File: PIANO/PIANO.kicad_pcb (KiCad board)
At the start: 2 copper layers, 71.6 x 47.5 mm, 31 parts, among them SW1 ON/OFF, SW2 RESET, U1 LF33_TO220, U2 ESP32-S2-SOLO, U3 Opamp_Dual, U4 Opamp_Dual

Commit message: During Class Commit
This contains all changes before design review
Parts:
- U1: value LF33_TO220 -> LDO 3.3V
- moved R2 2.18 mm to (153.5, 96.1)
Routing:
- net Net-(R2-Pad2): track 7.26 -> 15.8 mm, vias 0 -> 2
- net GND: track 0.00 -> 7.31 mm, vias 0 -> 4
- net Net-(C4-Pad1): track 15.9 -> 20.5 mm
- net /IO0: track 32.8 -> 37.0 mm
- net Net-(RV3-Pad2): track 35.9 -> 39.7 mm
- net Net-(R2-Pad1): track 19.5 -> 23.1 mm
- net +3V3: track 73.9 -> 76.6 mm
- net /Output: track 73.5 -> 76.0 mm
- net Net-(RV2-Pad2): track 16.4 -> 18.1 mm
- net +5V: track 66.6 -> 68.1 mm
- net Net-(C3-Pad2): track 24.3 -> 25.4 mm
- net /En: track 14.1 -> 13.4 mm

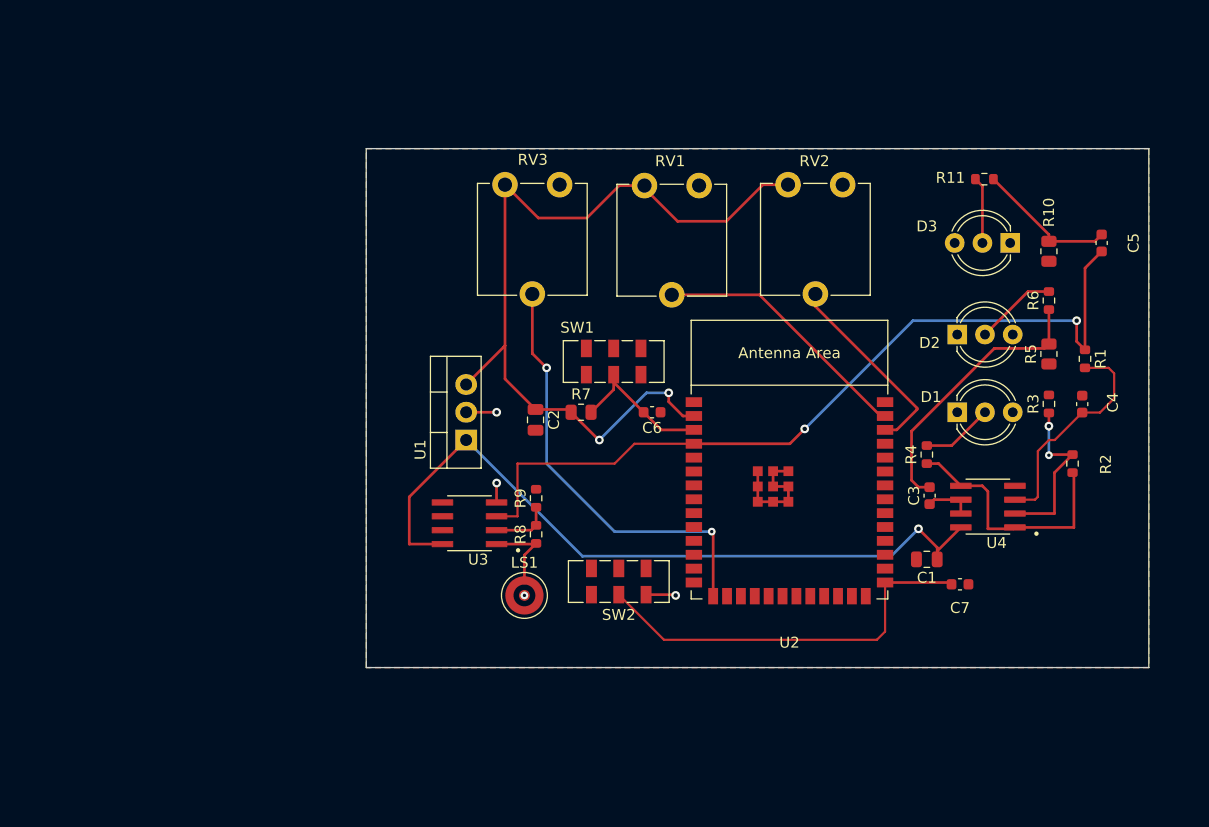
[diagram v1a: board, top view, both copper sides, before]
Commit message: Final Handoff to Wesley
Corrected units, created exclusion, thickened traces
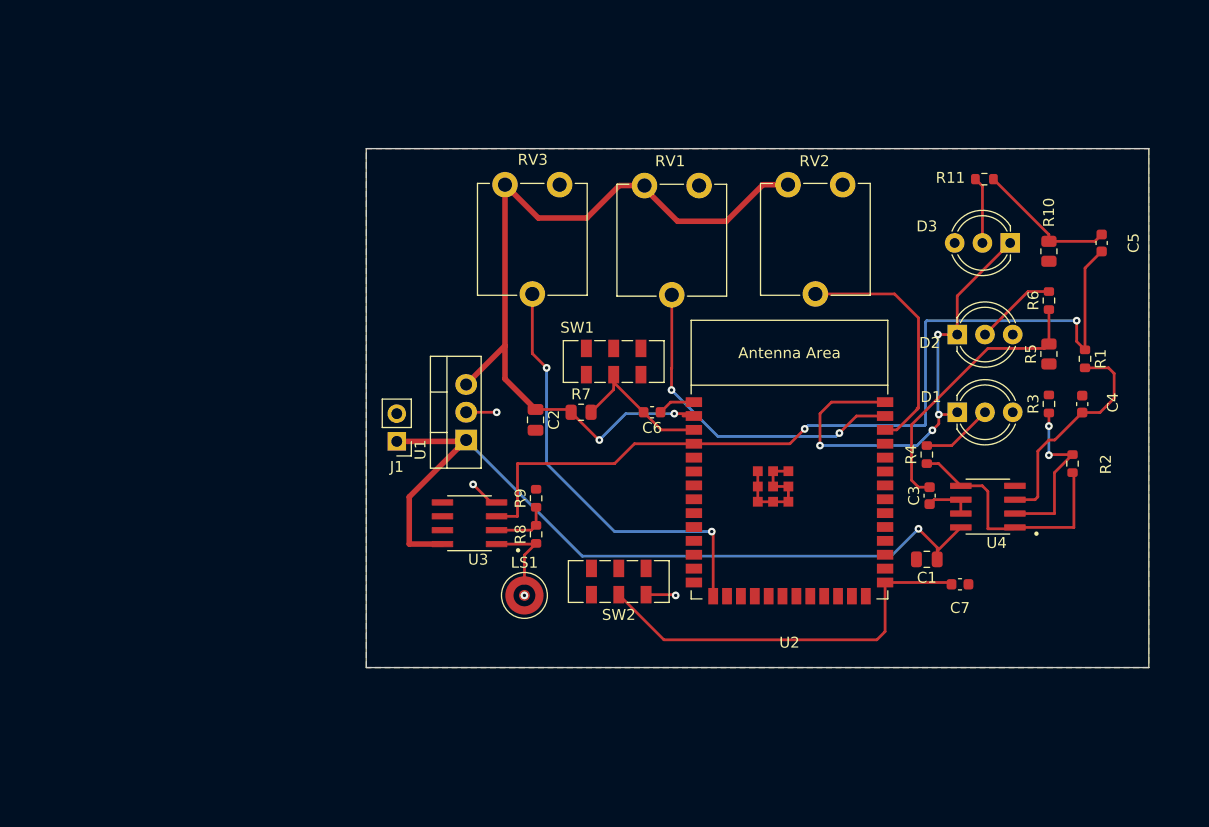
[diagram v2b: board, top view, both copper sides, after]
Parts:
- added J1: Conn_01x02_Male, Connector_PinHeader_2.54mm:PinHeader_1x02_P2.54mm_Vertical, F.Cu at (91.7, 94.1)
- C1, C2: value 10 mF -> 10 uF
- C3, C5, C6, C7: value .1 mF -> .1 uF
- C4: value .4 mF -> .4 uF
- U1: value LDO 3.3V -> LF33_TO220
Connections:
- U2 pad 40: unconnected-(U2-Pad40) -> GND
- U2 pad 41: unconnected-(U2-Pad41) -> GND
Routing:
- net GND: track 7.31 -> 66.5 mm, vias 4 -> 8
- net unconnected-(U2-Pad41): track 11.2 -> 0.00 mm
- net Net-(RV1-Pad2): track 24.1 -> 30.8 mm, vias 0 -> 2
- net +5V: track 68.1 -> 74.5 mm
- net /Output: track 76.0 -> 81.5 mm
- net Net-(RV2-Pad2): track 18.1 -> 22.6 mm
- net +3V3: track 76.6 -> 75.6 mm

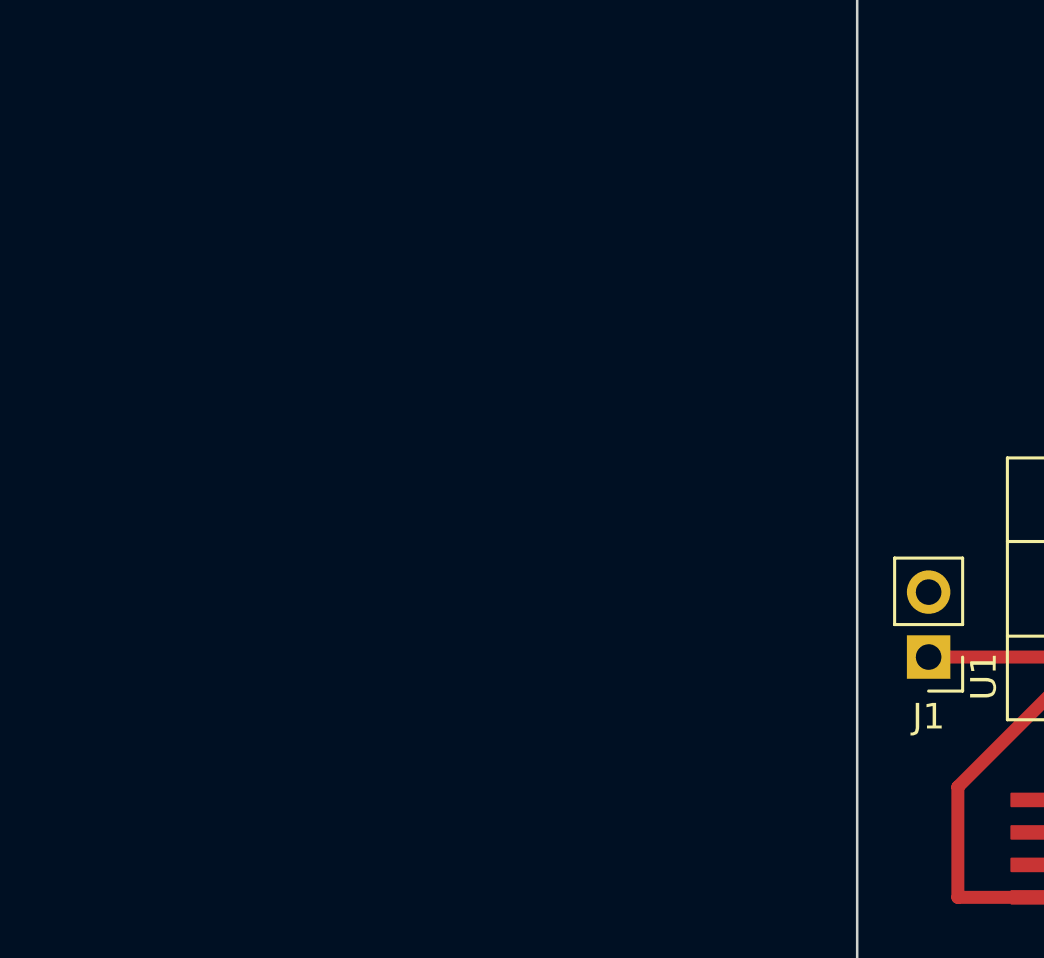
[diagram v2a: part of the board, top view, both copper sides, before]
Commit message: New Power Delivery
Created new switching regulator and respective passives.
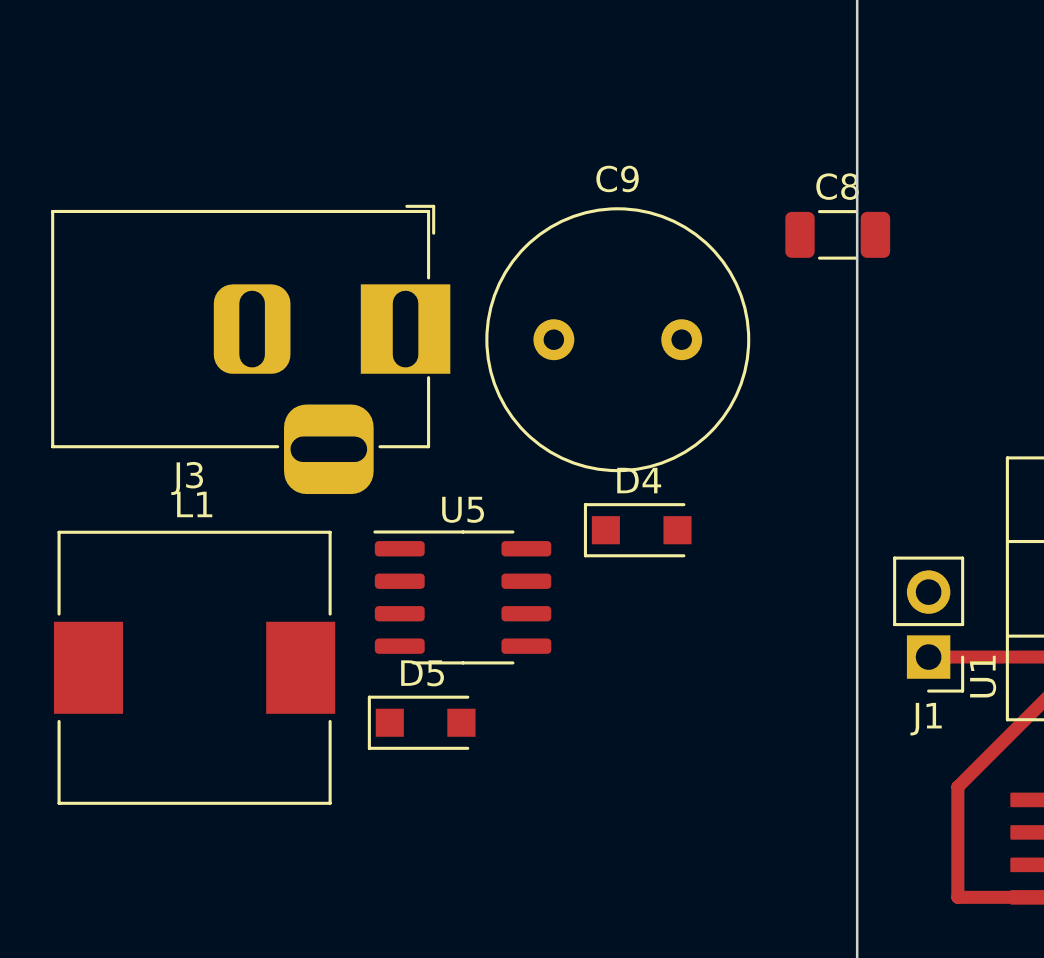
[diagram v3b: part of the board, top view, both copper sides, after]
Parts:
- added C8: 330uF, Capacitor_SMD:C_1206_3216Metric, F.Cu at (88.1, 77.6)
- added C9: 1000uF, Capacitor_THT:C_Radial_D10.0mm_H16.0mm_P5.00mm, F.Cu at (77.0, 81.7)
- added D4: DIODE, Diode_SMD:D_SOD-123F, F.Cu at (80.5, 89.1)
- added D5: D_Schottky, Diode_SMD:D_SOD-123F, F.Cu at (72.0, 96.7)
- added J3: Barrel_Jack_Switch, Connector_BarrelJack:BarrelJack_Horizontal, F.Cu at (71.2, 81.3)
- added L1: 39uH, Inductor_SMD:L_10.4x10.4_H4.8, F.Cu at (63.0, 94.5)
- added U5: AP1509-50SG-13, Package_SO:SOIC-8_3.9x4.9mm_P1.27mm, F.Cu at (73.5, 91.8)
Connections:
- U3 pad 8: +5V -> Net-(U3-Pad8)

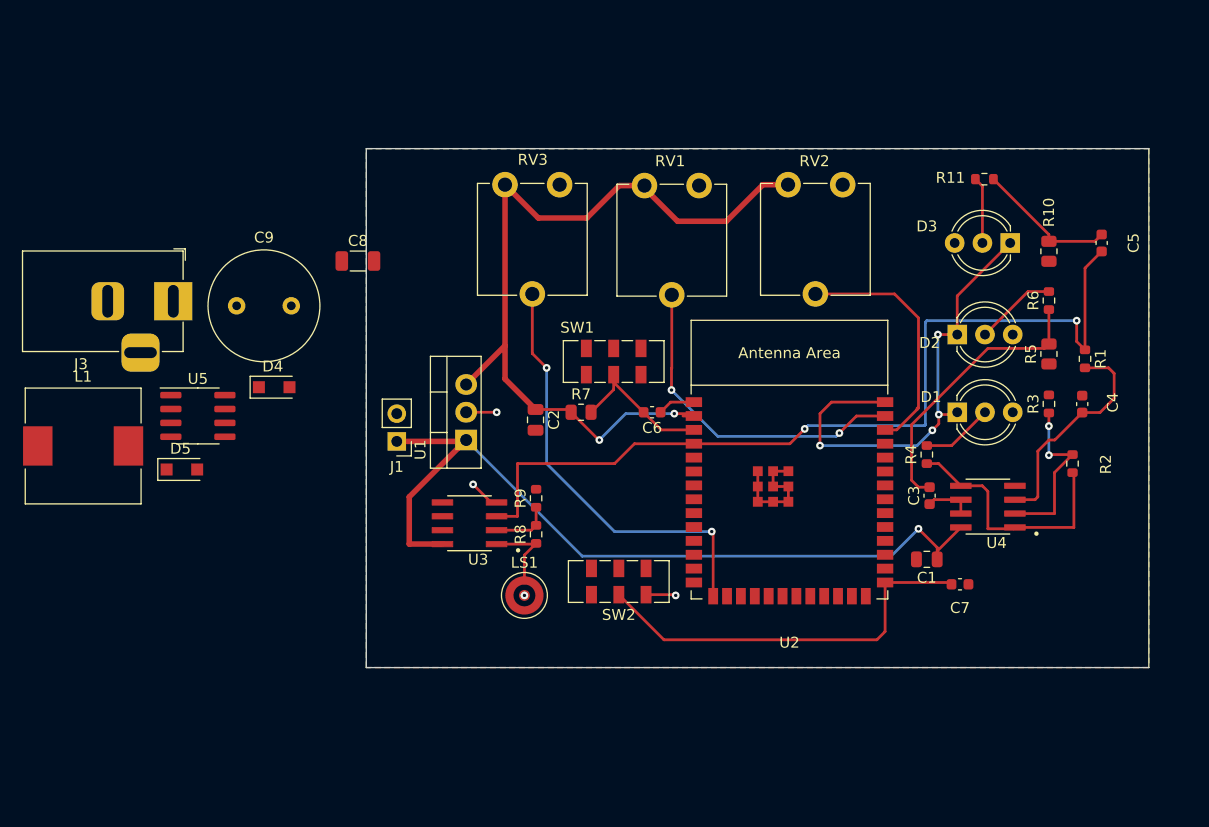
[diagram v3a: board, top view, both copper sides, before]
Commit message: added usb component
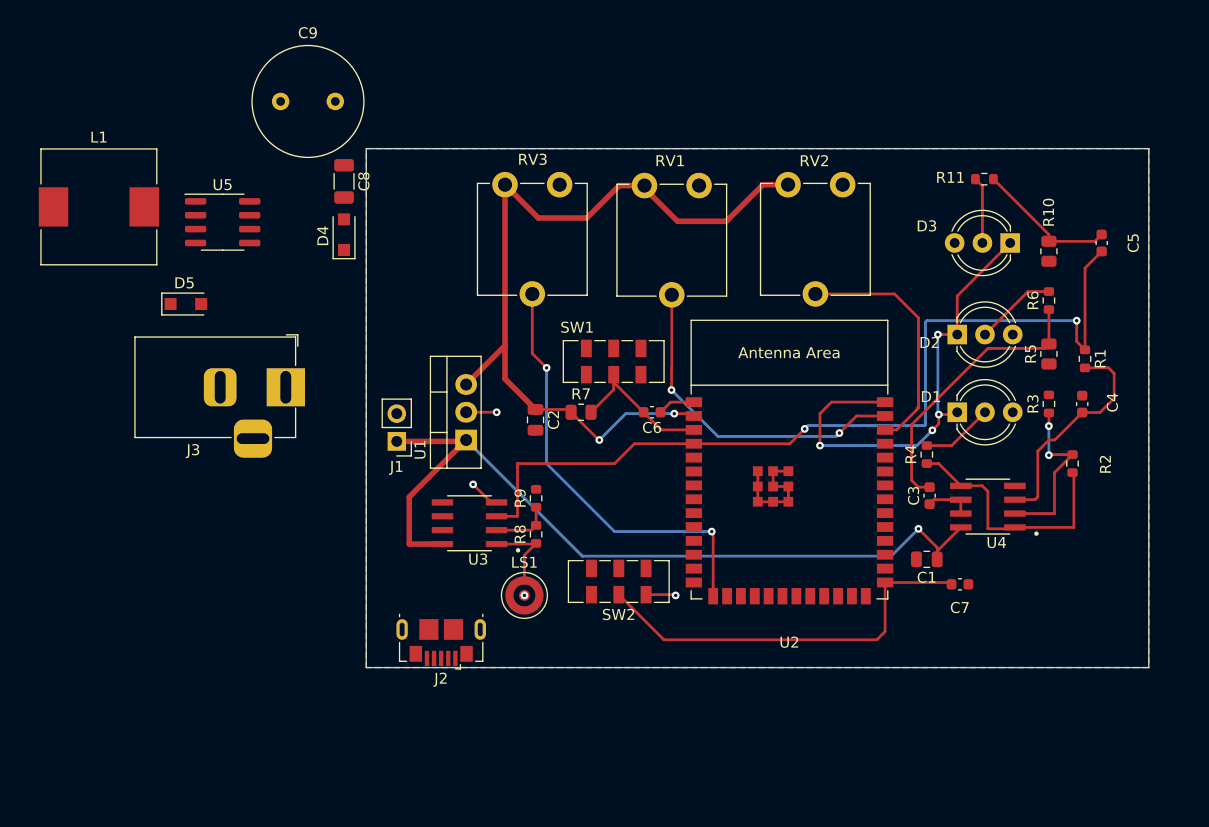
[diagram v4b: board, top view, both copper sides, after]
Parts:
- added J2: USB_B_Micro, Connector_USB:USB_Micro-B_GCT_USB3076-30-A, F.Cu at (95.8, 112.5)
- moved L1 21.9 mm to (64.4, 72.6)
- moved C9 19.1 mm to (81.1, 63.0)
- moved U5 17.9 mm to (75.8, 74.0)
- moved D4 15.4 mm to (86.9, 75.2), turned to 90 degrees
- moved D5 15.1 mm to (72.4, 81.5)
- moved J3 13.0 mm to (81.5, 89.2)
- moved C8 7.40 mm to (86.9, 70.3), turned to -90 degrees
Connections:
- U2 pad 13: unconnected-(U2-Pad13) -> /D-
- U2 pad 14: unconnected-(U2-Pad14) -> /D+
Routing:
- net +3V3: track 75.6 -> 74.6 mm

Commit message: added some stuff
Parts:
- moved J2 1.00 mm to (95.8, 111.5), turned to 0 degrees
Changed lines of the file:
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@@
   )
   (footprint "Connector_USB:USB_Micro-B_GCT_USB3076-30-A" (layer "F.Cu")
-    (at 95.758 112.522 180)
+    (at 95.758 111.52)
     (descr "GCT Micro USB https://gct.co/files/drawings/usb3076.pdf")
     (tags "Micro-USB SMD Typ-B GCT")
@@
     (fp_line (start -1.1 -2.16) (end -1.1 -1.95) (layer "F.Fab") (width 0.1))
     (fp_line (start -1.5 -2.16) (end -1.5 -1.95) (layer "F.Fab") (width 0.1))
-    (pad "1" smd rect (at -1.3 -1.45 180) (size 0.4 1.4) (layers "F.Cu" "F.Paste" "F.Mask")
+    (pad "1" smd rect (at -1.3 -1.45) (size 0.4 1.4) (layers "F.Cu" "F.Paste" "F.Mask")
       (net 1 "+5V") (pinfunction "VBUS") (pintype "power_out"))
-    (pad "2" smd rect (at -0.65 -1.45 180) (size 0.4 1.4) (layers "F.Cu" "F.Paste" "F.Mask")
+    (pad "2" smd rect (at -0.65 -1.45) (size 0.4 1.4) (layers "F.Cu" "F.Paste" "F.Mask")
       (net 21 "/D-") (pinfunction "D-") (pintype "bidirectional"))
-    (pad "3" smd rect (at 0 -1.45 180) (size 0.4 1.4) (layers "F.Cu" "F.Paste" "F.Mask")
+    (pad "3" smd rect (at 0 -1.45) (size 0.4 1.4) (layers "F.Cu" "F.Paste" "F.Mask")
       (net 22 "/D+") (pinfunction "D+") (pintype "bidirectional"))
-    (pad "4" smd rect (at 0.65 -1.45 180) (size 0.4 1.4) (layers "F.Cu" "F.Paste" "F.Mask")
+    (pad "4" smd rect (at 0.65 -1.45) (size 0.4 1.4) (layers "F.Cu" "F.Paste" "F.Mask")
       (net 59 "unconnected-(J2-Pad4)") (pinfunction "ID") (pintype "passive+no_connect"))
-    (pad "5" smd rect (at 1.3 -1.45 180) (size 0.4 1.4) (layers "F.Cu" "F.Paste" "F.Mask")
+    (pad "5" smd rect (at 1.3 -1.45) (size 0.4 1.4) (layers "F.Cu" "F.Paste" "F.Mask")
       (net 2 "GND") (pinfunction "GND") (pintype "power_out"))
-    (pad "6" thru_hole oval (at 3.575 1.2 180) (size 1.05 1.9) (drill oval 0.45 1.25) (layers *.Cu *.Mask)
+    (pad "6" thru_hole oval (at 3.575 1.2) (size 1.05 1.9) (drill oval 0.45 1.25) (layers *.Cu *.Mask)
       (net 2 "GND") (pinfunction "Shield") (pintype "passive"))
-    (pad "6" thru_hole oval (at -3.575 1.2) (size 1.05 1.9) (drill oval 0.45 1.25) (layers *.Cu *.Mask)
+    (pad "6" thru_hole oval (at -3.575 1.2 180) (size 1.05 1.9) (drill oval 0.45 1.25) (layers *.Cu *.Mask)
       (net 2 "GND") (pinfunction "Shield") (pintype "passive"))
-    (pad "6" smd rect (at 2.32 -1.03 180) (size 1.15 1.45) (layers "F.Cu" "F.Paste" "F.Mask")
+    (pad "6" smd rect (at 2.32 -1.03) (size 1.15 1.45) (layers "F.Cu" "F.Paste" "F.Mask")
       (net 2 "GND") (pinfunction "Shield") (pintype "passive"))
-    (pad "6" smd rect (at -2.32 -1.03 180) (size 1.15 1.45) (layers "F.Cu" "F.Paste" "F.Mask")
+    (pad "6" smd rect (at -2.32 -1.03) (size 1.15 1.45) (layers "F.Cu" "F.Paste" "F.Mask")
       (net 2 "GND") (pinfunction "Shield") (pintype "passive"))
-    (pad "6" smd rect (at -1.125 1.2 180) (size 1.75 1.9) (layers "F.Cu" "F.Paste" "F.Mask")
+    (pad "6" smd rect (at -1.125 1.2) (size 1.75 1.9) (layers "F.Cu" "F.Paste" "F.Mask")
       (net 2 "GND") (pinfunction "Shield") (pintype "passive"))
-    (pad "6" smd rect (at 1.125 1.2 180) (size 1.75 1.9) (layers "F.Cu" "F.Paste" "F.Mask")
+    (pad "6" smd rect (at 1.125 1.2) (size 1.75 1.9) (layers "F.Cu" "F.Paste" "F.Mask")
       (net 2 "GND") (pinfunction "Shield") (pintype "passive"))
     (model "${KICAD6_3DMODEL_DIR}/Connector_USB.3dshapes/USB_Micro-B_GCT_USB3076-30-A.wrl"

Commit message: need to final check
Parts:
- removed LS1: Speaker, Sensor_Audio:CUI_CMC-4013-SMT
- added C10: 10 uF, Capacitor_SMD:C_0805_2012Metric, F.Cu at (79.0, 74.4)
- added C11: 10 uF, Capacitor_SMD:C_0805_2012Metric, F.Cu at (72.6, 74.2)
- added C12: 10 uF, Capacitor_SMD:C_0805_2012Metric, F.Cu at (85.8, 74.7)
- added J1: 640456-3, Connector_PinHeader_1.00mm:PinHeader_1x03_P1.00mm_Vertical, F.Cu at (80.0, 70.6)
- added J4: 22-23-2021, Connector_PinHeader_1.00mm:PinHeader_1x02_P1.00mm_Vertical, F.Cu at (105.4, 106.2)
- added J5: 640456-3, Connector_PinHeader_1.00mm:PinHeader_1x03_P1.00mm_Vertical, F.Cu at (73.4, 70.6)
- added J6: 640456-3, Connector_PinHeader_1.00mm:PinHeader_1x03_P1.00mm_Vertical, F.Cu at (86.6, 70.6)
- moved C8 33.3 mm to (93.3, 103.0)
- moved D5 30.2 mm to (82.9, 109.9), turned to -90 degrees
- moved U5 30.1 mm to (85.7, 102.5), turned to 180 degrees
- moved D4 30.1 mm to (98.4, 103.0)
- moved J3 29.9 mm to (100.7, 112.1)
- moved SW2 29.1 mm to (140.2, 114.3)
- moved C9 20.4 mm to (86.9, 82.5)
- moved L1 17.5 mm to (76.5, 85.3)
- moved J2 17.0 mm to (112.5, 114.6)
- moved U3 13.7 mm to (112.0, 100.6)
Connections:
- net 9V renamed +9V
- C9 pad 1: 5V -> +5V
- D5 pad 1: 5V -> +5V
- J2 pad 1: +5V -> unconnected-(J2-Pad1)
- L1 pad 1: 5V -> +5V
- L1 pad 2: 5V -> +5V
- U2 pad 12: unconnected-(U2-Pad12) -> /Strip3
- U2 pad 5: unconnected-(U2-Pad5) -> /Spkr 1
- U2 pad 6: unconnected-(U2-Pad6) -> /Strip1
- U2 pad 7: unconnected-(U2-Pad7) -> /Strip2
- U3 pad 3: /Output -> /Spkr 1
- U3 pad 8: Net-(U3-Pad8) -> +5V
- U5 pad 2: 5V -> +5V
- U5 pad 3: 5V -> +5V
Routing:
- net +5V: track 74.5 -> 139.5 mm, vias 1 -> 2
- net /Output: track 81.5 -> 56.6 mm
- net /IO0: track 37.0 -> 15.4 mm
- net /D-: track 0.00 -> 11.8 mm
- net +9V: track 0.00 -> 11.4 mm
- net /D+: track 0.00 -> 10.7 mm
- net Net-(D4-Pad1): track 0.00 -> 8.66 mm
- net Net-(J4-Pad2): track 7.39 -> 15.2 mm
- net /Spkr 1: track 0.00 -> 7.05 mm
- net Net-(R8-Pad2): track 5.46 -> 11.9 mm
- net GND: track 66.5 -> 60.6 mm, vias 8 -> 5
- net /3 LED_STRIPS/Strip3: track 0.00 -> 4.36 mm
- net /3 LED_STRIPS/Strip1: track 0.00 -> 4.20 mm
- net /3 LED_STRIPS/Strip2: track 0.00 -> 3.90 mm
- net Net-(R2-Pad1): track 23.1 -> 19.7 mm
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- removed copper zone on B.Cu, net GND
- removed copper zone on F.Cu, net GND
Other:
- board outline removed
